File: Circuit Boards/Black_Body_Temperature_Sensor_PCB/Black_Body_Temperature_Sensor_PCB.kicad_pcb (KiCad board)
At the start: 6 copper layers, 60 x 74 mm, 108 parts, among them J401 Screw_Terminal_01x02, J402 Screw_Terminal_01x02, J701 Conn_01x06_Pin, J702 5040500891, J703 USB_C_Receptacle_USB2.0_16P, P601 436500200, P701 pogo programmer, Q201 TMUX1112PWR, Q202 TMUX1112PWR, Q301 TMUX1112PWR, Q401 TMUX1112PWR, Q402 TMUX1112PWR, Q403 TMUX1112PWR, SW701 SW_MEC_5E, SW702 SW_MEC_5E, U201 LM334M, U301 LM334M, U302 LT1008, U501 OPA376xxDBV, U502 OPA376xxDBV, U503 OPA376xxDBV, U504 OPA376xxDBV, U505 AD8421ARZ, U506 AD8421ARZ, U507 ADS131M04xPW, U510 OPA376xxDBV, U511 ISO7762FDBQ, U601 LTC3260xMSE, U602 LT3094xMSE, U603 LT3042xMSE, U701 TXU0304, U702 ABM8G-25.000MHZ-18-D2Y-T, U703 USBLC6-2SC6, U704 STM32G431RBTx, U705 AMS1117-3.3

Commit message: Digital section done
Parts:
- added C501: 220nf, Capacitor_SMD:C_0603_1608Metric, F.Cu at (203.1, 84.8)
- added J601: Conn_01x02_Pin, Connector_PinHeader_2.54mm:PinHeader_1x02_P2.54mm_Vertical, F.Cu at (185.4, 56.6)
- J401, J402: footprint TerminalBlock_MetzConnect:TerminalBlock_MetzConnect_Type011_RT05502HBLC_1x02_P5.00mm_Horizontal -> -connector:CUI_TB002-500-02BE
- moved R614 13.2 mm to (189.2, 80.2), turned to 0 degrees
- moved R609 12.2 mm to (179.8, 70.6), turned to 0 degrees
- moved R613 11.2 mm to (189.2, 78.7), turned to 180 degrees
- moved C610 11.2 mm to (184.7, 79.4), turned to -90 degrees
- moved R605 11.1 mm to (186.2, 79.4), turned to 90 degrees
- moved C608 9.96 mm to (182.5, 73.1), turned to -90 degrees
- moved R606 7.91 mm to (177.2, 73.8), turned to 90 degrees
- moved C612 6.67 mm to (182.5, 76.1), turned to -90 degrees
- moved U603 6.49 mm to (179.8, 74.7), turned to -90 degrees
- moved C609 4.95 mm to (188.9, 70.4), turned to 0 degrees
- moved U602 4.61 mm to (186.8, 74.6), turned to -90 degrees
- moved R612 4.17 mm to (181.5, 80.6), turned to 180 degrees
- moved R611 3.66 mm to (181.5, 79.1), turned to 0 degrees
- moved R607 3.09 mm to (186.7, 69.7), turned to 90 degrees
- moved R610 2.77 mm to (185.2, 69.7), turned to -90 degrees
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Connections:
- net /V&I_sense/AIN2N renamed /V&I_sense/sense_iso_V-
- U505 pad 7: /V&I_sense/AIN0P -> /V&I_sense/AIN1P
- U506 pad 7: /V&I_sense/AIN1P -> /V&I_sense/AIN0P
- U507 pad 18: unconnected-(U507-CAP-Pad18) -> /V&I_sense/cap
- U704 pad 10: /micrcontroller/i_sense_sel3 -> /micrcontroller/i_sense_sel2
- U704 pad 11: /micrcontroller/i_sense_sel4 -> /micrcontroller/i_sense_sel3
- U704 pad 22: unconnected-(U704-PC4-Pad22) -> /micrcontroller/i_sense_sel4
- U704 pad 34: /V&I_sense/SPI.CS -> /micrcontroller/CS
- U704 pad 35: /V&I_sense/SPI.SCLK -> /micrcontroller/CLK
- U704 pad 36: /V&I_sense/SPI.MISO -> /micrcontroller/MISO
- U704 pad 37: /V&I_sense/SPI.MOSI -> /micrcontroller/MOSI
- U704 pad 39: /V&I_sense/ADC_DRDY -> unconnected-(U704-PC7-Pad39)
- U704 pad 51: /micrcontroller/CS -> /V&I_sense/SPI.CS
- U704 pad 52: /micrcontroller/CLK -> /V&I_sense/SPI.SCLK
- U704 pad 53: /micrcontroller/MISO -> /V&I_sense/SPI.MISO
- U704 pad 54: /micrcontroller/MOSI -> /V&I_sense/SPI.MOSI
- U704 pad 8: /micrcontroller/i_sense_sel1 -> /V&I_sense/ADC_DRDY
- U704 pad 9: /micrcontroller/i_sense_sel2 -> /micrcontroller/i_sense_sel1
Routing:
- net /micrcontroller/NRST: track 0.00 -> 42.2 mm, vias 0 -> 5
- net /micrcontroller/BOOT0: track 3.80 -> 38.3 mm, vias 0 -> 2
- net /V&I_sense/SPI.MOSI: track 0.00 -> 17.8 mm, vias 0 -> 2
- net /V&I_sense/SPI.SCLK: track 0.00 -> 17.7 mm, vias 0 -> 2
- net /V&I_sense/CLK_MCO: track 0.00 -> 17.6 mm, vias 0 -> 2
- net /V&I_sense/SPI.CS: track 0.00 -> 17.2 mm, vias 0 -> 2
- net /micrcontroller/MOSI: track 0.00 -> 17.0 mm, vias 0 -> 2
- net /V&I_sense/SPI.MISO: track 0.00 -> 15.9 mm, vias 0 -> 2
- net /V&I_sense/sense_iso_V-: track 8.53 -> 23.4 mm
- net /micrcontroller/MISO: track 0.00 -> 13.3 mm, vias 0 -> 2
- net /micrcontroller/CLK: track 0.00 -> 12.9 mm, vias 0 -> 2
- net Net-(U507-CLKIN): track 0.00 -> 11.7 mm
- net /micrcontroller/CS: track 0.00 -> 10.1 mm, vias 0 -> 2
- net /V&I_sense/AIN1P: track 0.00 -> 9.12 mm
- net Net-(U507-~{DRDY}): track 0.00 -> 8.59 mm, vias 0 -> 2
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- added copper zone on B.Cu, net +5VA
- added copper zone on B.Cu, net -5VA
- added copper zone on B.Cu, net 12Vin
- added copper zone on F.Cu, net 12Vin
- added copper zone on In1.Cu, net GND
- added copper zone on In4.Cu, net GND
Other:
- board size 60 x 74 mm -> 60 x 75.2 mm

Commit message: Complete except for recommended changes
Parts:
- added C201: 2u2, Capacitor_SMD:C_0402_1005Metric, F.Cu at (194.6, 77.5)
- added C202: 2u2, Capacitor_SMD:C_0402_1005Metric, F.Cu at (198.6, 77.5)
- added C203: 2u2, Capacitor_SMD:C_0402_1005Metric, F.Cu at (202.6, 77.5)
- added C204: 2u2, Capacitor_SMD:C_0402_1005Metric, F.Cu at (196.6, 77.5)
- added C205: 2u2, Capacitor_SMD:C_0402_1005Metric, F.Cu at (219.8, 70.8)
- added C206: 2u2, Capacitor_SMD:C_0402_1005Metric, F.Cu at (204.6, 77.5)
- added C207: 2u2, Capacitor_SMD:C_0402_1005Metric, F.Cu at (200.6, 77.5)
- added C208: 2u2, Capacitor_SMD:C_0402_1005Metric, F.Cu at (217.8, 70.8)
- added C209: 2u2, Capacitor_SMD:C_0402_1005Metric, F.Cu at (194.1, 76.1)
- added C210: 2u2, Capacitor_SMD:C_0402_1005Metric, F.Cu at (198.1, 76.1)
- added C211: 2u2, Capacitor_SMD:C_0402_1005Metric, F.Cu at (202.1, 76.1)
- added C212: 2u2, Capacitor_SMD:C_0402_1005Metric, F.Cu at (196.1, 76.1)
- added C213: 2u2, Capacitor_SMD:C_0402_1005Metric, F.Cu at (219.3, 69.4)
- added C214: 2u2, Capacitor_SMD:C_0402_1005Metric, F.Cu at (204.1, 76.1)
- added C215: 2u2, Capacitor_SMD:C_0402_1005Metric, F.Cu at (200.1, 76.1)
- added C216: 2u2, Capacitor_SMD:C_0402_1005Metric, F.Cu at (217.3, 69.4)
- added C301: 2u2, Capacitor_SMD:C_0402_1005Metric, F.Cu at (221.8, 70.8)
- added C302: 2u2, Capacitor_SMD:C_0402_1005Metric, F.Cu at (216.9, 74.1)
- added C303: 2u2, Capacitor_SMD:C_0402_1005Metric, F.Cu at (220.8, 74.1)
- added C304: 2u2, Capacitor_SMD:C_0402_1005Metric, F.Cu at (218.9, 74.1)
- added C305: 2u2, Capacitor_SMD:C_0402_1005Metric, F.Cu at (221.3, 69.4)
- added C306: 2u2, Capacitor_SMD:C_0402_1005Metric, F.Cu at (216.4, 72.7)
- added C307: 2u2, Capacitor_SMD:C_0402_1005Metric, F.Cu at (220.3, 72.7)
- added C308: 2u2, Capacitor_SMD:C_0402_1005Metric, F.Cu at (218.4, 72.7)
- added C401: 2u2, Capacitor_SMD:C_0402_1005Metric, F.Cu at (220.0, 77.5)
- added C402: 2u2, Capacitor_SMD:C_0402_1005Metric, F.Cu at (222.0, 77.5)
- added C403: 2u2, Capacitor_SMD:C_0402_1005Metric, F.Cu at (224.0, 77.5)
- added C404: 2u2, Capacitor_SMD:C_0402_1005Metric, F.Cu at (228.0, 77.5)
- added C405: 2u2, Capacitor_SMD:C_0402_1005Metric, F.Cu at (219.5, 76.1)
- added C406: 2u2, Capacitor_SMD:C_0402_1005Metric, F.Cu at (221.5, 76.1)
- added C407: 2u2, Capacitor_SMD:C_0402_1005Metric, F.Cu at (223.5, 76.1)
- added C408: 2u2, Capacitor_SMD:C_0402_1005Metric, F.Cu at (227.5, 76.1)
- added C409: 2u2, Capacitor_SMD:C_0402_1005Metric, F.Cu at (232.0, 77.5)
- added C410: 2u2, Capacitor_SMD:C_0402_1005Metric, F.Cu at (234.0, 77.5)
- added C411: 2u2, Capacitor_SMD:C_0402_1005Metric, F.Cu at (230.0, 77.5)
- added C412: 2u2, Capacitor_SMD:C_0402_1005Metric, F.Cu at (226.0, 77.5)
- added C413: 2u2, Capacitor_SMD:C_0402_1005Metric, F.Cu at (231.5, 76.1)
- added C414: 2u2, Capacitor_SMD:C_0402_1005Metric, F.Cu at (233.5, 76.1)
- added C415: 2u2, Capacitor_SMD:C_0402_1005Metric, F.Cu at (229.5, 76.1)
- added C416: 2u2, Capacitor_SMD:C_0402_1005Metric, F.Cu at (225.5, 76.1)
- added C417: 2u2, Capacitor_SMD:C_0402_1005Metric, F.Cu at (222.8, 74.1)
- added C418: 2u2, Capacitor_SMD:C_0402_1005Metric, F.Cu at (216.0, 77.5)
- added C419: 2u2, Capacitor_SMD:C_0402_1005Metric, F.Cu at (218.0, 77.5)
- added C420: 2u2, Capacitor_SMD:C_0402_1005Metric, F.Cu at (214.0, 77.5)
- added C421: 2u2, Capacitor_SMD:C_0402_1005Metric, F.Cu at (222.3, 72.7)
- added C422: 2u2, Capacitor_SMD:C_0402_1005Metric, F.Cu at (215.5, 76.1)
- added C423: 2u2, Capacitor_SMD:C_0402_1005Metric, F.Cu at (217.5, 76.0)
- added C424: 2u2, Capacitor_SMD:C_0402_1005Metric, F.Cu at (213.5, 76.1)
- added R201: 5.1k, Resistor_SMD:R_0402_1005Metric, F.Cu at (193.6, 77.5)
- added R202: 5.1k, Resistor_SMD:R_0402_1005Metric, F.Cu at (197.6, 77.5)
- added R203: 5.1k, Resistor_SMD:R_0402_1005Metric, F.Cu at (201.6, 77.5)
- added R204: 5.1k, Resistor_SMD:R_0402_1005Metric, F.Cu at (195.6, 77.5)
- added R205: 5.1k, Resistor_SMD:R_0402_1005Metric, F.Cu at (218.8, 70.8)
- added R206: 5.1k, Resistor_SMD:R_0402_1005Metric, F.Cu at (203.6, 77.5)
- added R207: 5.1k, Resistor_SMD:R_0402_1005Metric, F.Cu at (199.6, 77.5)
- added R208: 5.1k, Resistor_SMD:R_0402_1005Metric, F.Cu at (216.8, 70.8)
- added R301: 5.1k, Resistor_SMD:R_0402_1005Metric, F.Cu at (220.8, 70.8)
- added R302: 5.1k, Resistor_SMD:R_0402_1005Metric, F.Cu at (215.9, 74.1)
- added R303: 5.1k, Resistor_SMD:R_0402_1005Metric, F.Cu at (219.8, 74.1)
- added R304: 5.1k, Resistor_SMD:R_0402_1005Metric, F.Cu at (217.9, 74.1)
- added R401: 5.1k, Resistor_SMD:R_0402_1005Metric, F.Cu at (219.0, 77.5)
- added R402: 5.1k, Resistor_SMD:R_0402_1005Metric, F.Cu at (221.0, 77.5)
- added R403: 5.1k, Resistor_SMD:R_0402_1005Metric, F.Cu at (223.0, 77.5)
- added R404: 5.1k, Resistor_SMD:R_0402_1005Metric, F.Cu at (227.0, 77.5)
- added R408: 5.1k, Resistor_SMD:R_0402_1005Metric, F.Cu at (231.0, 77.5)
- added R409: 5.1k, Resistor_SMD:R_0402_1005Metric, F.Cu at (233.0, 77.5)
- added R410: 5.1k, Resistor_SMD:R_0402_1005Metric, F.Cu at (229.0, 77.5)
- added R411: 5.1k, Resistor_SMD:R_0402_1005Metric, F.Cu at (225.0, 77.5)
- added R414: 5.1k, Resistor_SMD:R_0402_1005Metric, F.Cu at (221.8, 74.1)
- added R415: 5.1k, Resistor_SMD:R_0402_1005Metric, F.Cu at (215.0, 77.5)
- added R416: 5.1k, Resistor_SMD:R_0402_1005Metric, F.Cu at (217.0, 77.5)
- added R417: 5.1k, Resistor_SMD:R_0402_1005Metric, F.Cu at (213.0, 77.5)
- added TP401: TestPoint, TestPoint:TestPoint_Pad_2.0x2.0mm, F.Cu at (211.7, 116.3)
- added TP402: TestPoint, TestPoint:TestPoint_Pad_2.0x2.0mm, F.Cu at (199.8, 102.4)
- added TP403: TestPoint, TestPoint:TestPoint_Pad_2.0x2.0mm, F.Cu at (200.6, 118.8)
- added TP601: TestPoint, TestPoint:TestPoint_Pad_2.0x2.0mm, F.Cu at (179.0, 84.2)
- added TP602: TestPoint, TestPoint:TestPoint_Pad_2.0x2.0mm, F.Cu at (179.0, 101.0)
- added TP603: TestPoint, TestPoint:TestPoint_Pad_2.0x2.0mm, F.Cu at (186.0, 49.5)
- D201: value 1N357 -> 1N457
- R701, R702: footprint Resistor_SMD:R_0603_1608Metric -> Resistor_SMD:R_0402_1005Metric
- moved R701 0.50 mm to (202.0, 55.0), turned to 0 degrees
- moved R702 0.30 mm to (202.0, 53.9)
- renumbered C301 to C309, C705 to C704, C706 to C705, C708 to C706, C709 to C708, C710 to C711, C713 to C712, C714 to C713, C715 to C714, C716 to C715, R201 to R209, R202 to R210, R203 to R211, R204 to R212, R205 to R213, R206 to R214, R207 to R215, R208 to R216, R301 to R305, R302 to R306, R303 to R307, R304 to R308, R305 to R309, R306 to R310, R307 to R311, R401 to R405, R402 to R406, R403 to R407, R404 to R412, R405 to R413, R703 to R704, R704 to R705, U511 to U508, U510 to U509
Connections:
- P701 pad 3: /micrcontroller/swclk -> GNDPWR
- P701 pad 4: GNDPWR -> /micrcontroller/swclk
- Q201 pad 1: /micrcontroller/sel_v.10uA -> /uA_current/selv1
- Q201 pad 16: /micrcontroller/sel_v.1uA -> /uA_current/selv2
- Q201 pad 8: /micrcontroller/sel_v.100uA -> /uA_current/selv4
- Q201 pad 9: /micrcontroller/sel_v.1mA -> /uA_current/selv3
- Q202 pad 1: /micrcontroller/sel_t.1uA -> /uA_current/selt1
- Q202 pad 16: /micrcontroller/sel_t.10uA -> /uA_current/selt2
- Q202 pad 8: /micrcontroller/sel_t.1mA -> /uA_current/selt4
- Q202 pad 9: /micrcontroller/sel_t.100uA -> /uA_current/selt3
- Q301 pad 1: /micrcontroller/sel.100na_neg -> /nA_current/sel1
- Q301 pad 16: /micrcontroller/sel.10na_neg -> /nA_current/sel2
- Q301 pad 8: /micrcontroller/sel.10na_pos -> /nA_current/sel4
- Q301 pad 9: /micrcontroller/sel.100na_pos -> /nA_current/sel3
- Q401 pad 1: /micrcontroller/i_sense_sel1 -> /sensor_interface/seli1
- Q401 pad 16: /micrcontroller/i_sense_sel2 -> /sensor_interface/seli2
- Q401 pad 8: /micrcontroller/i_sense_sel4 -> /sensor_interface/seli4
- Q401 pad 9: /micrcontroller/i_sense_sel3 -> /sensor_interface/seli3
- Q402 pad 1: /micrcontroller/hbridge_sel1 -> /sensor_interface/selh1
- Q402 pad 16: /micrcontroller/hbridge_sel2 -> /sensor_interface/selh2
- Q402 pad 8: /micrcontroller/hbridge_sel4 -> /sensor_interface/selh4
- Q402 pad 9: /micrcontroller/hbridge_sel3 -> /sensor_interface/selh3
- Q403 pad 1: /micrcontroller/i_source_sel1 -> /sensor_interface/sels1
- Q403 pad 16: /micrcontroller/i_source_sel2 -> /sensor_interface/sels2
- Q403 pad 8: /micrcontroller/i_source_sel4 -> /sensor_interface/sels4
- Q403 pad 9: /micrcontroller/i_source_sel3 -> /sensor_interface/sels3
- R701 pad 1: /micrcontroller/CC1 -> GNDPWR
- R701 pad 2: GNDPWR -> /micrcontroller/CC1
- U704 pad 10: /micrcontroller/i_sense_sel2 -> /micrcontroller/i_source_sel2
- U704 pad 11: /micrcontroller/i_sense_sel3 -> /micrcontroller/i_sense_sel1
- U704 pad 12: /micrcontroller/i_source_sel1 -> /micrcontroller/i_sense_sel2
- U704 pad 13: /micrcontroller/i_source_sel2 -> /micrcontroller/i_sense_sel3
- U704 pad 14: /micrcontroller/i_source_sel3 -> /micrcontroller/hbridge_sel4
- U704 pad 17: /micrcontroller/i_source_sel4 -> /micrcontroller/i_sense_sel4
- U704 pad 18: /micrcontroller/sel_t.1mA -> /micrcontroller/hbridge_sel3
- U704 pad 19: /micrcontroller/sel_t.100uA -> /micrcontroller/hbridge_sel1
- U704 pad 2: unconnected-(U704-PC13-Pad2) -> /micrcontroller/sel_v.1mA
- U704 pad 20: /micrcontroller/sel_t.10uA -> /micrcontroller/hbridge_sel2
- U704 pad 21: /micrcontroller/sel_t.1uA -> /micrcontroller/sel.10na_pos
- U704 pad 22: /micrcontroller/i_sense_sel4 -> /micrcontroller/sel.100na_pos
- U704 pad 23: unconnected-(U704-PC5-Pad23) -> /micrcontroller/i_source_sel1
- U704 pad 24: /micrcontroller/sel_v.10uA -> /micrcontroller/sel.100na_neg
- U704 pad 25: /micrcontroller/sel_v.1uA -> /micrcontroller/sel_t.1mA
- U704 pad 26: unconnected-(U704-PB2-Pad26) -> /micrcontroller/sel_t.1uA
- U704 pad 33: /micrcontroller/sel.10na_pos -> unconnected-(U704-PB11-Pad33)
- U704 pad 4: unconnected-(U704-PC15-Pad4) -> /micrcontroller/i_source_sel4
- U704 pad 43: /micrcontroller/sel_v.1mA -> unconnected-(U704-PA9-Pad43)
- U704 pad 44: /micrcontroller/sel_v.100uA -> unconnected-(U704-PA10-Pad44)
- U704 pad 55: unconnected-(U704-PD2-Pad55) -> /micrcontroller/sel_v.10uA
- U704 pad 56: /micrcontroller/hbridge_sel1 -> unconnected-(U704-PB3-Pad56)
- U704 pad 57: /micrcontroller/hbridge_sel2 -> /micrcontroller/sel_v.100uA
- U704 pad 58: /micrcontroller/hbridge_sel3 -> /micrcontroller/sel_v.1uA
- U704 pad 59: /micrcontroller/hbridge_sel4 -> unconnected-(U704-PB6-Pad59)
- U704 pad 60: /micrcontroller/sel.100na_neg -> /micrcontroller/sel_t.100uA
- U704 pad 62: /micrcontroller/sel.100na_pos -> /micrcontroller/sel_t.10uA
- U704 pad 9: /micrcontroller/i_sense_sel1 -> /micrcontroller/i_source_sel3
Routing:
- net GNDPWR: track 8.70 -> 201.2 mm, vias 52 -> 83
- net +3V3: track 8.68 -> 161.7 mm, vias 41 -> 51
- net /nA_current/sel1: track 0.00 -> 69.0 mm, vias 0 -> 3
- net /nA_current/sel4: track 0.00 -> 67.3 mm, vias 0 -> 2
- net /nA_current/sel3: track 0.00 -> 58.7 mm, vias 0 -> 3
- net /sensor_interface/selh2: track 0.00 -> 58.2 mm, vias 0 -> 2
- net /sensor_interface/selh3: track 0.00 -> 56.1 mm, vias 0 -> 2
- net /nA_current/sel2: track 0.00 -> 55.1 mm, vias 0 -> 2
- net /uA_current/selt1: track 0.00 -> 54.5 mm, vias 0 -> 3
- net /sensor_interface/seli4: track 0.00 -> 48.1 mm, vias 0 -> 2
- net /sensor_interface/selh1: track 0.00 -> 47.8 mm, vias 0 -> 2
- net /uA_current/selt4: track 0.00 -> 46.7 mm, vias 0 -> 3
- net /sensor_interface/sels1: track 0.00 -> 43.2 mm, vias 0 -> 3
- net /sensor_interface/sels3: track 0.00 -> 41.1 mm, vias 0 -> 2
- net /sensor_interface/sels4: track 0.00 -> 41.0 mm, vias 0 -> 2
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- added copper zone on In2.Cu, net +3V3A
- added copper zone on In3.Cu, net -3V3A

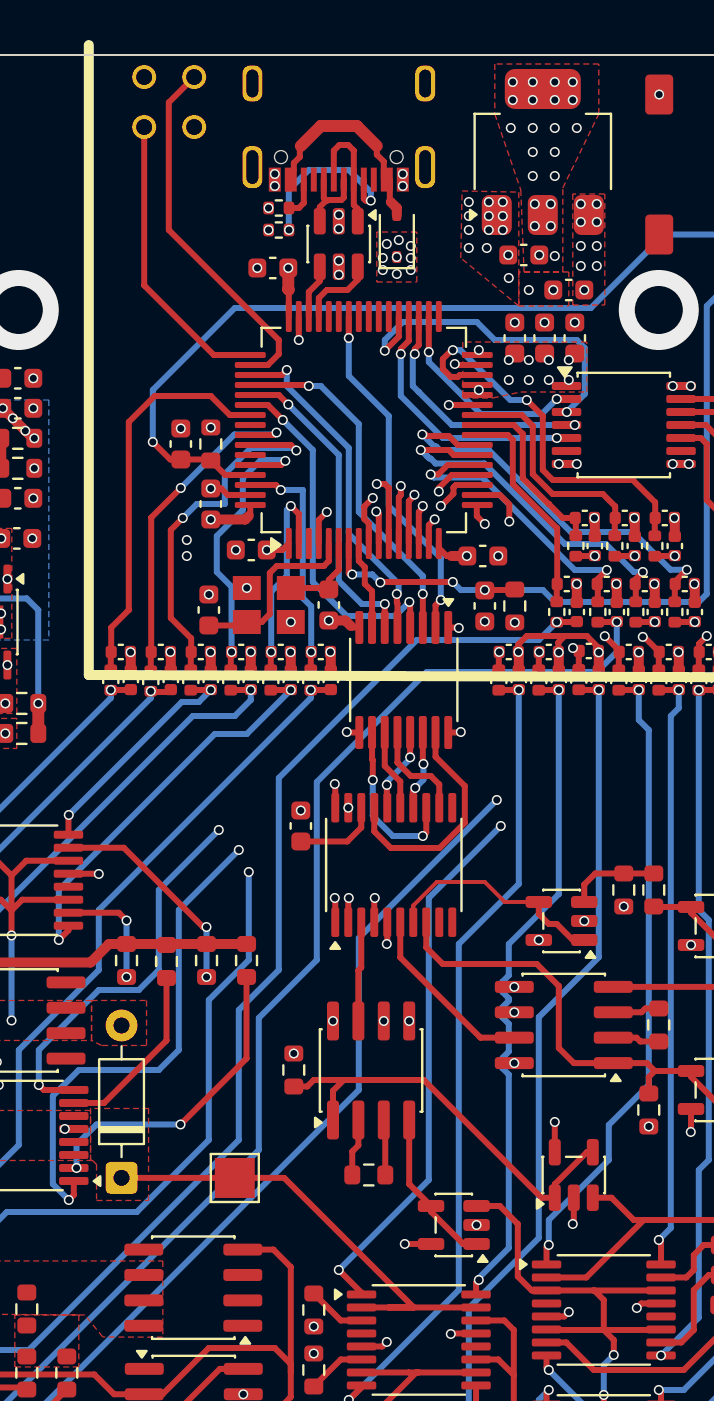
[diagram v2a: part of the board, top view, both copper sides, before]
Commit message: Heater switched from pwm to vccs
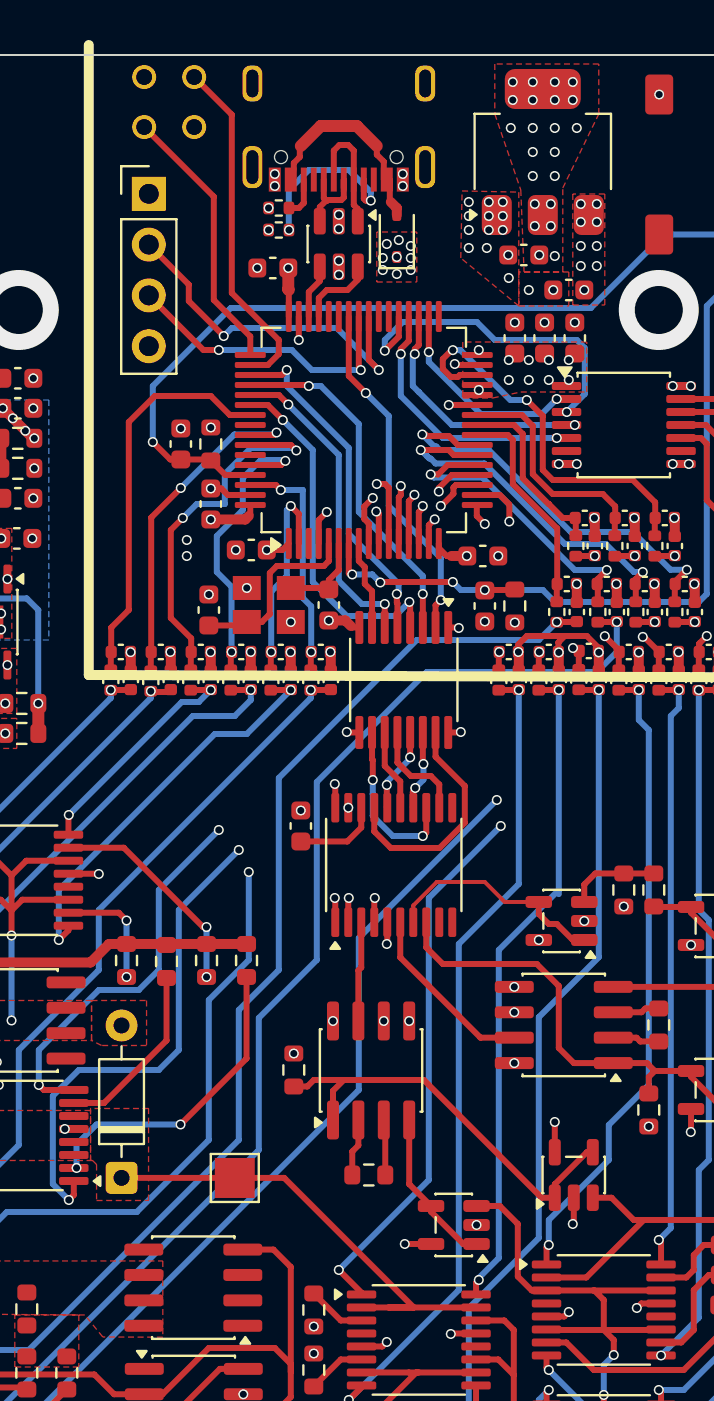
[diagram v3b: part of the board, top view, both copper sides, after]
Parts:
- added J704: Conn_01x04_Pin, Connector_PinHeader_2.54mm:PinHeader_1x04_P2.54mm_Vertical, F.Cu at (195.5, 53.2)
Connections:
- U704 pad 40: unconnected-(U704-PC8-Pad40) -> /micrcontroller/SCL
- U704 pad 41: unconnected-(U704-PC9-Pad41) -> /micrcontroller/SDA
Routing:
- net /micrcontroller/SCL: track 0.00 -> 17.8 mm, vias 0 -> 2
- net /micrcontroller/SDA: track 0.00 -> 14.9 mm, vias 0 -> 2
- net /micrcontroller/swdio: track 14.7 -> 13.6 mm
- net /micrcontroller/swclk: track 18.3 -> 17.3 mm
- net /sensor_interface/sels2: track 33.8 -> 33.2 mm
